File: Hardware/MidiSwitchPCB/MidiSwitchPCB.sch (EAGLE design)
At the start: 11 parts, among them IC1 74AHC1G04DBV, IC2 74AHC1G04DBV

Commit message: continued schematic designing
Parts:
- added C1: (no value), rcl:C-EUC0603
- added C2: (no value), rcl:CPOL-EU153CLV-1012
- added CN5: (no value), pinhead:PINHD-1X10
- added CN6, CN7: (no value), pinhead:PINHD-1X8
- added CN8: (no value), pinhead:PINHD-1X6
- added D2, D3, D4, D5, D6, D7, D8, D9: (no value), diode:DIODE-DO-214AC
- added K1, K2, K3, K4, K5, K6, K7, K8: APF30212C, relay:APF30212C
- added Q1, Q2, Q3, Q4, Q5, Q6, Q7, Q8: BSS123, transistor-small-signal:BSS123
- added R10, R11, R12, R13, R6, R7, R8, R9: (no value), rcl:R-EU_R0603
- added U1: MAX1627ESA, Max1627:MAX1627ESA
- added X1, X2, X3, X4: 1503_09, con-lumberg:1503_09
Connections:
- new net N$12: D2.A, K11.2, Q1.D
- new net N$13: D3.A, K31.2, Q2.D
- new net N$14: Q1.G, R6.2
- new net N$15: Q2.G, R7.2
- new net N$16: D4.A, K41.2, Q3.D
- new net N$17: Q3.G, R8.2
- new net N$18: CN7.4, R7.1
- new net N$19: K32.S, X2.5
- new net N$20: D6.A, K21.2, Q5.D
- new net N$21: Q5.G, R10.2
- new net N$22: K42.S, X2.2
- new net N$23: K32.O, K32.P, K42.O, K42.P, X2.1
- new net N$24: D5.A, K51.2, Q4.D
- new net N$25: Q4.G, R9.2
- new net N$26: D7.A, K61.2, Q6.D
- new net N$27: Q6.G, R11.2
- new net N$28: CN7.2, R9.1
- new net N$29: K52.S, X3.5
- new net N$30: K62.S, X3.2
- new net N$31: CN7.6, R6.1
- new net N$32: K52.O, K52.P, K62.O, K62.P, X3.1
- new net N$33: D8.A, K71.2, Q7.D
- new net N$34: Q7.G, R12.2
- new net N$35: D9.A, K81.2, Q8.D
- new net N$36: K12.S, X1.5
- new net N$37: K22.S, X1.2
- new net N$38: K12.O, K12.P, K22.O, K22.P, X1.1
- new net N$39: Q8.G, R13.2
- new net N$40: CN7.1, R12.1
- new net N$41: K72.S, X4.5
- new net N$42: K82.S, X4.2
- new net N$43: K72.O, K72.P, K82.O, K82.P, X4.1
- new net N$44: CN7.8, R13.1
- new net N$45: CN5.2, R8.1
- new net N$46: CN7.7, R11.1
- new net N$47: CN5.1, R10.1
- net GND: now also C1.2, C2.-, Q1.S, Q2.S, Q3.S, Q4.S, Q5.S, Q6.S, Q7.S, Q8.S
- net N$9: now also CN7.3
- net VCC: now also C1.1, C2.+, CN6.8, D2.C, D3.C, D4.C, D5.C, D6.C, D7.C, D8.C, D9.C, K11.1, K21.1, K31.1, K41.1, K51.1, K61.1, K71.1, K81.1

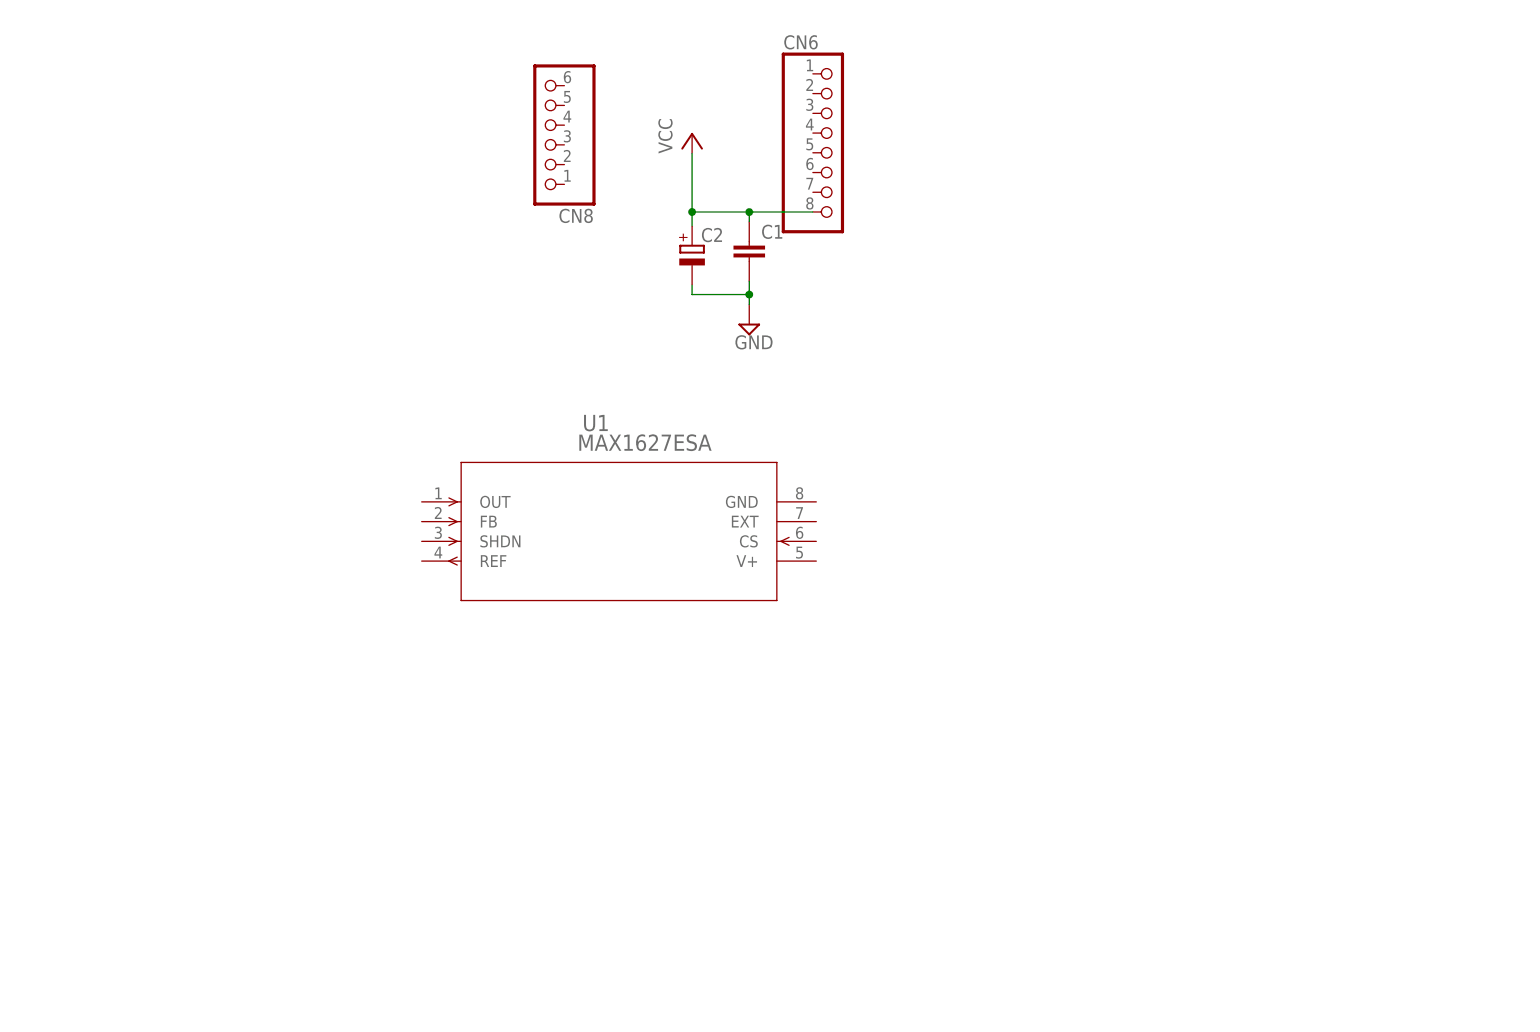
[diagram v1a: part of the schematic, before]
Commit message: added most of the power supply.
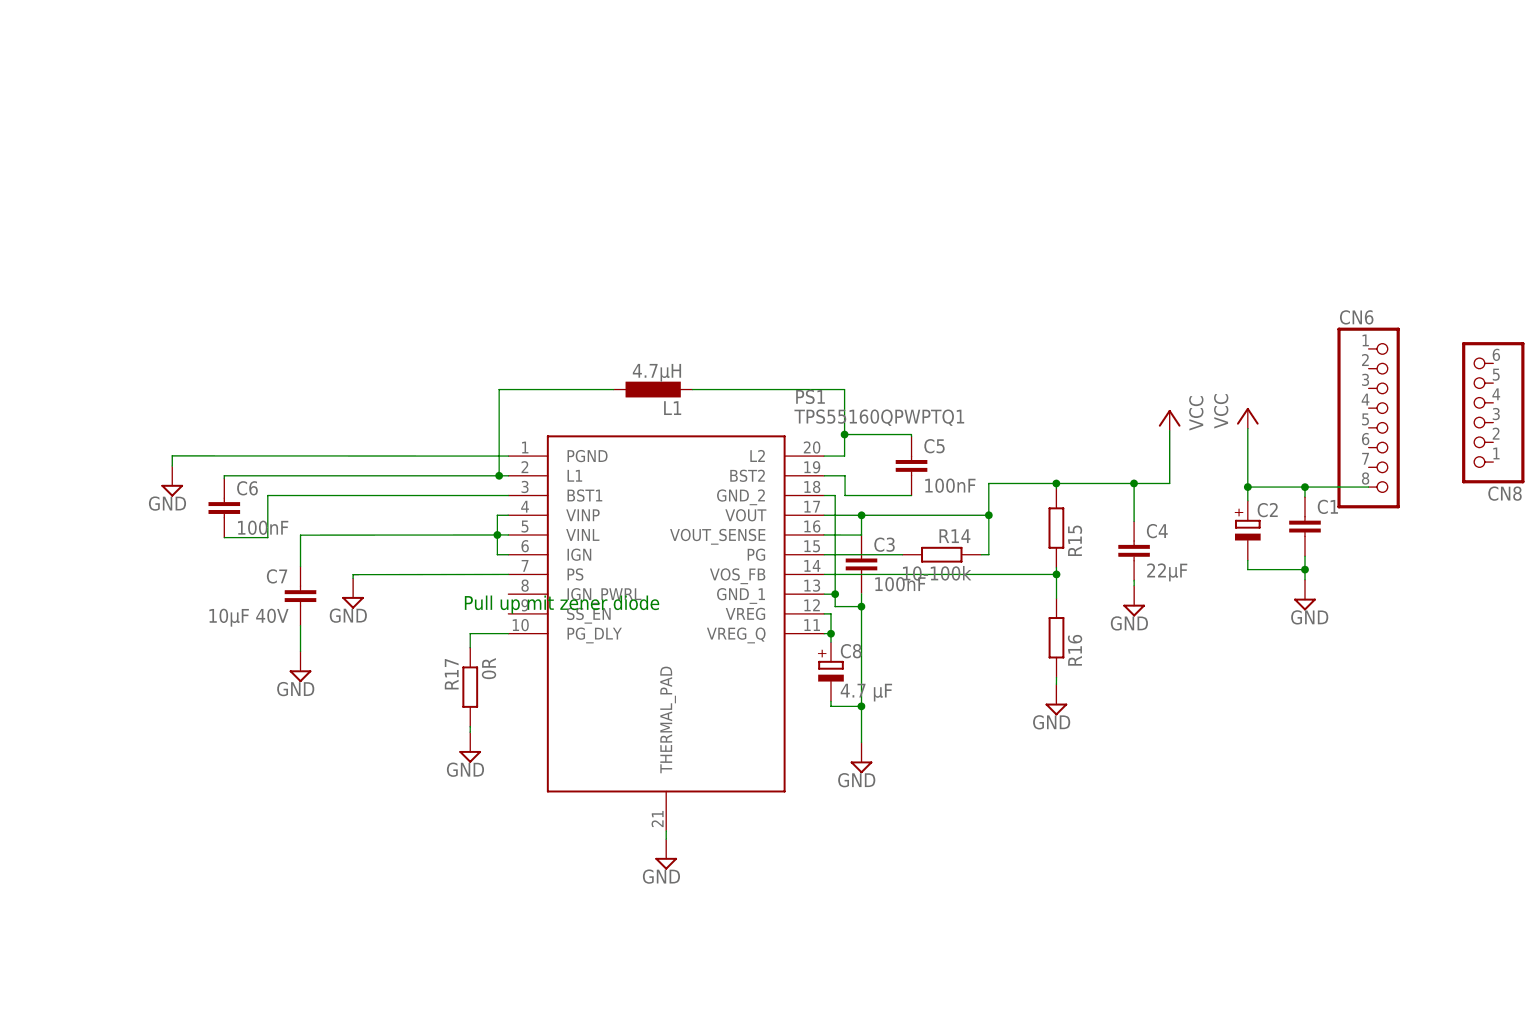
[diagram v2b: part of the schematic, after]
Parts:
- removed U1: MAX1627ESA, Max1627:MAX1627ESA
- added C3, C5, C6: 100nF, rcl:C-EUC0603
- added C4: 22µF, rcl:C-EUC0603
- added C7: 10µF 40V, rcl:C-EUC0603
- added C8: 4.7 µF, rcl:CPOL-EU153CLV-1012
- added L1: 4.7µH, rcl:L-EUWE-TPC
- added PS1: TPS55160QPWPTQ1, TPS55160QPWPTQ1:TPS55160QPWPTQ1
- added R14: 10-100k, rcl:R-EU_R0603
- added R15, R16: (no value), rcl:R-EU_R0603
- added R17: 0R, rcl:R-EU_R0603
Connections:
- new net N$48: PS1.PG_DLY, R17.1
- new net N$49: PS1.VOS_FB, R16.2
- new net N$50: R15.1
- new net N$51: C5.1, L1.2, PS1.L2
- new net N$52: PS1.PG, R14.2
- new net N$53: C7.1, PS1.IGN, PS1.VINL, PS1.VINP
- new net N$54: C5.2, PS1.BST2
- new net N$55: C6.1, L1.1, PS1.L1
- new net N$56: C6.2, PS1.BST1
- new net N$57: C8.+, PS1.VREG, PS1.VREG_Q
- net GND: now also C3.2, C4.2, C7.2, C8.-, PS1.GND_1, PS1.GND_2, PS1.PGND, PS1.PS, PS1.THERMAL_PAD, R16.1, R17.2
- net VCC: now also C3.1, C4.1, PS1.VOUT, PS1.VOUT_SENSE, R14.1, R15.2
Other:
- note added: "Pull up mit zener diode"
- moved on the sheet: C1, C2, CN6, CN8

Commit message: created the part list and selected some devices
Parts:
- OK1: value 6N138 -> HCPL0500; device optocoupler:6N138 -> optocoupler:HCPL0500
- R10, R11, R12, R13, R6, R7, R8, R9: value (none) -> 220
- R15: value (none) -> 800k
- R16: value (none) -> 100k
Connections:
- net GND: now also OK1.GND
- net N$8: now also D1.A
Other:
- moved on the sheet: R4, R5

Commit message: added switching capacitor to part list (changed cap-package in layout from 0603 to 1206)
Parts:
- C5, C6: device rcl:C-EUC0603 -> rcl:C-EUC1206
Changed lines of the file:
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@@
 <setting verticaltext="up"/>
 </settings>
-<grid distance="0.01" unitdist="mm" unit="mm" style="lines" multiple="1" display="no" altdistance="0.01" altunitdist="mm" altunit="mm"/>
+<grid distance="0.1" unitdist="inch" unit="inch" style="lines" multiple="1" display="no" altdistance="0.01" altunitdist="inch" altunit="inch"/>
 <layers>
-<layer number="1" name="Top" color="4" fill="1" visible="yes" active="no"/>
-<layer number="2" name="Route2" color="1" fill="3" visible="yes" active="no"/>
-<layer number="3" name="Route3" color="4" fill="3" visible="yes" active="no"/>
-<layer number="4" name="Route4" color="1" fill="4" visible="yes" active="no"/>
-<layer number="5" name="Route5" color="4" fill="4" visible="yes" active="no"/>
-<layer number="6" name="Route6" color="1" fill="8" visible="yes" active="no"/>
-<layer number="7" name="Route7" color="4" fill="8" visible="yes" active="no"/>
-<layer number="8" name="Route8" color="1" fill="2" visible="yes" active="no"/>
-<layer number="9" name="Route9" color="4" fill="2" visible="yes" active="no"/>
-<layer number="10" name="Route10" color="1" fill="7" visible="yes" active="no"/>
-<layer number="11" name="Route11" color="4" fill="7" visible="yes" active="no"/>
-<layer number="12" name="Route12" color="1" fill="5" visible="yes" active="no"/>
-<layer number="13" name="Route13" color="4" fill="5" visible="yes" active="no"/>
-<layer number="14" name="Route14" color="1" fill="6" visible="yes" active="no"/>
-<layer number="15" name="Route15" color="4" fill="6" visible="yes" active="no"/>
-<layer number="16" name="Bottom" color="1" fill="1" visible="yes" active="no"/>
-<layer number="17" name="Pads" color="2" fill="1" visible="yes" active="no"/>
-<layer number="18" name="Vias" color="2" fill="1" visible="yes" active="no"/>
-<layer number="19" name="Unrouted" color="6" fill="1" visible="yes" active="no"/>
-<layer number="20" name="Dimension" color="15" fill="1" visible="yes" active="no"/>
-<layer number="21" name="tPlace" color="7" fill="1" visible="yes" active="no"/>
-<layer number="22" name="bPlace" color="7" fill="1" visible="yes" active="no"/>
-<layer number="23" name="tOrigins" color="15" fill="1" visible="yes" active="no"/>
-<layer number="24" name="bOrigins" color="15" fill="1" visible="yes" active="no"/>
-<layer number="25" name="tNames" color="7" fill="1" visible="yes" active="no"/>
-<layer number="26" name="bNames" color="7" fill="1" visible="yes" active="no"/>
-<layer number="27" name="tValues" color="7" fill="1" visible="yes" active="no"/>
-<layer number="28" name="bValues" color="7" fill="1" visible="yes" active="no"/>
+<layer number="1" name="Top" color="4" fill="1" visible="no" active="no"/>
+<layer number="2" name="Route2" color="1" fill="3" visible="no" active="no"/>
+<layer number="3" name="Route3" color="4" fill="3" visible="no" active="no"/>
+<layer number="4" name="Route4" color="1" fill="4" visible="no" active="no"/>
+<layer number="5" name="Route5" color="4" fill="4" visible="no" active="no"/>
+<layer number="6" name="Route6" color="1" fill="8" visible="no" active="no"/>
+<layer number="7" name="Route7" color="4" fill="8" visible="no" active="no"/>
+<layer number="8" name="Route8" color="1" fill="2" visible="no" active="no"/>
+<layer number="9" name="Route9" color="4" fill="2" visible="no" active="no"/>
+<layer number="10" name="Route10" color="1" fill="7" visible="no" active="no"/>
+<layer number="11" name="Route11" color="4" fill="7" visible="no" active="no"/>
+<layer number="12" name="Route12" color="1" fill="5" visible="no" active="no"/>
+<layer number="13" name="Route13" color="4" fill="5" visible="no" active="no"/>
+<layer number="14" name="Route14" color="1" fill="6" visible="no" active="no"/>
+<layer number="15" name="Route15" color="4" fill="6" visible="no" active="no"/>
+<layer number="16" name="Bottom" color="1" fill="1" visible="no" active="no"/>
+<layer number="17" name="Pads" color="2" fill="1" visible="no" active="no"/>
+<layer number="18" name="Vias" color="2" fill="1" visible="no" active="no"/>
+<layer number="19" name="Unrouted" color="6" fill="1" visible="no" active="no"/>
+<layer number="20" name="Dimension" color="15" fill="1" visible="no" active="no"/>
+<layer number="21" name="tPlace" color="7" fill="1" visible="no" active="no"/>
+<layer number="22" name="bPlace" color="7" fill="1" visible="no" active="no"/>
+<layer number="23" name="tOrigins" color="15" fill="1" visible="no" active="no"/>
+<layer number="24" name="bOrigins" color="15" fill="1" visible="no" active="no"/>
+<layer number="25" name="tNames" color="7" fill="1" visible="no" active="no"/>
+<layer number="26" name="bNames" color="7" fill="1" visible="no" active="no"/>
+<layer number="27" name="tValues" color="7" fill="1" visible="no" active="no"/>
+<layer number="28" name="bValues" color="7" fill="1" visible="no" active="no"/>
 <layer number="29" name="tStop" color="7" fill="3" visible="no" active="no"/>
 <layer number="30" name="bStop" color="7" fill="6" visible="no" active="no"/>
@@
 <layer number="35" name="tGlue" color="7" fill="4" visible="no" active="no"/>
 <layer number="36" name="bGlue" color="7" fill="5" visible="no" active="no"/>
-<layer number="37" name="tTest" color="7" fill="1" visible="yes" active="no"/>
-<layer number="38" name="bTest" color="7" fill="1" visible="yes" active="no"/>
+<layer number="37" name="tTest" color="7" fill="1" visible="no" active="no"/>
+<layer number="38" name="bTest" color="7" fill="1" visible="no" active="no"/>
 <layer number="39" name="tKeepout" color="4" fill="11" visible="no" active="no"/>
 <layer number="40" name="bKeepout" color="1" fill="11" visible="no" active="no"/>
@@
 <layer number="44" name="Drills" color="7" fill="1" visible="no" active="no"/>
 <layer number="45" name="Holes" color="7" fill="1" visible="no" active="no"/>
-<layer number="46" name="Milling" color="3" fill="1" visible="yes" active="no"/>
-<layer number="47" name="Measures" color="7" fill="1" visible="yes" active="no"/>
-<layer number="48" name="Document" color="7" fill="1" visible="yes" active="no"/>
-<layer number="49" name="Reference" color="7" fill="1" visible="yes" active="no"/>
-<layer number="51" name="tDocu" color="7" fill="1" visible="yes" active="no"/>
-<layer number="52" name="bDocu" color="7" fill="1" visible="yes" active="no"/>
+<layer number="46" name="Milling" color="3" fill="1" visible="no" active="no"/>
+<layer number="47" name="Measures" color="7" fill="1" visible="no" active="no"/>
+<layer number="48" name="Document" color="7" fill="1" visible="no" active="no"/>
+<layer number="49" name="Reference" color="7" fill="1" visible="no" active="no"/>
+<layer number="51" name="tDocu" color="7" fill="1" visible="no" active="no"/>
+<layer number="52" name="bDocu" color="7" fill="1" visible="no" active="no"/>
 <layer number="90" name="Modules" color="5" fill="1" visible="yes" active="yes"/>
 <layer number="91" name="Nets" color="2" fill="1" visible="yes" active="yes"/>
@@
 <part name="C4" library="rcl" deviceset="C-EU" device="C0603" value="22µF"/>
 <part name="SUPPLY16" library="supply2" deviceset="GND" device=""/>
-<part name="C5" library="rcl" deviceset="C-EU" device="C0603" value="100nF"/>
-<part name="C6" library="rcl" deviceset="C-EU" device="C0603" value="100nF"/>
+<part name="C5" library="rcl" deviceset="C-EU" device="C1206" value="100nF"/>
+<part name="C6" library="rcl" deviceset="C-EU" device="C1206" value="100nF"/>
 <part name="L1" library="rcl" deviceset="L-EU" device="WE-TPC" value="4.7µH"/>
 <part name="C7" library="rcl" deviceset="C-EU" device="C0603" value="10µF 40V"/>

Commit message: added some part libraries
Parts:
- removed IC1, IC2: 74AHC1G04DBV, 74xx-little-de:74AHC1G04DBV
- added IC3: 74LVC2G04GW,125, 74LVC2G04GW_125:74LVC2G04GW,125
- added R18, R19: 0R, rcl:R-EU_R0603
- C7: device rcl:C-EUC0603 -> rcl:CPOL-EU153CLV-0605
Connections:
- new net N$58: PS1.IGN_PWRL, R18.2, R19.1
- new net VCC_3_3: IC3.VCC, OK1.VCC, R3.2, R5.2
- new net VCC_6-8: C1.1, C2.+, C3.1, C4.1, CN6.8, D2.C, D3.C, D4.C, D5.C, D6.C, D7.C, D8.C, D9.C, K11.1, K21.1, K31.1, K41.1, K51.1, K61.1, K71.1, K81.1, PS1.VOUT, PS1.VOUT_SENSE, R14.1, R15.2
- net GND: now also C7.-, IC3.GND, R19.2; no longer C7.2
- net MIDI_RX: now also IC3.2A; no longer IC1A.I
- net N$1: now also IC3.1A, IC3.2Y; no longer IC1A.O, IC2A.I
- net N$11: now also IC3.1Y; no longer IC2A.O
- net N$53: now also C7.+, R18.1; no longer C7.1
- net VCC: now also CN6.4; no longer C1.1, C2.+, C3.1, C4.1, CN6.8, D2.C, D3.C, D4.C, D5.C, D6.C, D7.C, D8.C, D9.C, K11.1, K21.1, K31.1, K41.1, K51.1, K61.1, K71.1, K81.1, OK1.VCC, PS1.VOUT, PS1.VOUT_SENSE, R14.1, R15.2, R3.2, R5.2
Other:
- note removed: "Pull up mit zener diode"

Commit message: continued searching parts
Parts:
- added R20, R21, R22, R23, R24, R25, R26, R27: (no value), rcl:R-EU_R0603
- C4: device rcl:C-EUC0603 -> rcl:C-EUC1206
- C8: device rcl:CPOL-EU153CLV-1012 -> rcl:C-EUC0805
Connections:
- new net N$59: K11.1, R20.1
- new net N$60: K21.1, R22.1
- new net N$61: K31.1, R21.1
- new net N$62: K41.1, R23.1
- new net N$63: K51.1, R24.1
- new net N$64: K61.1, R25.1
- new net N$65: K71.1, R26.1
- new net N$66: K81.1, R27.1
- net GND: now also C8.2; no longer C8.-
- net N$57: now also C8.1; no longer C8.+
- net VCC_6-8: now also R20.2, R21.2, R22.2, R23.2, R24.2, R25.2, R26.2, R27.2; no longer K11.1, K21.1, K31.1, K41.1, K51.1, K61.1, K71.1, K81.1
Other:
- moved on the sheet: D2, D3, D4, D5, D6, D7, D8, D9, K1, K2, K3, K4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
